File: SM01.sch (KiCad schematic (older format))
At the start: 37 parts

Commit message: basic layout complete
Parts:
- removed J?: SynthOut, symbol JACK-MONO
- removed J?: DC JACK, symbol JACK-MONO
- removed R?: R, symbol R
- removed U? (x5): 74AHC1G14, symbol 74AHC1G14
- added ATTACK, ATTACK? (x2), DECAY, DECAY? (x2): A500k, symbol POT
- added C3, C?: 100uF, C-POL-5, symbol CAP-ELEC-TH
- added C? (x2): C, symbol C
- added C? (x3): 10uF, symbol C
- added C? (x10): 1uF, symbol C
- added C? (x5): .1uF, symbol C
- added C? (x2): .22uF, symbol C
- added C? (x4): 47pF, symbol C
- added D2, D? (x2): 4148, symbol D
- added D?: D, symbol D
- added J2, J? (x2): TRIG IN, symbol JACK-MONO
- added J?: VCA IN, symbol JACK-MONO
- added J?: EXP1, symbol JACK-MONO
- added J?: EXP2, symbol JACK-MONO
- added J?: EXP3, symbol JACK-MONO
- added LED? (x2): LED-C1-A2, LED-C1-A2-3MM-VERT, symbol LED-C1-A2
- added MOM1, SW4, SW? (x2): SPDT_small, symbol SPDT_small
- added OSC? (x2): 10k, symbol POT
- added Q?: 2N3904, TO_SOT_Packages_THT:TO-92_Molded_Narrow, symbol 2N3904
- added R1, R2, R? (x15): 100k, symbol R
- added R3, R? (x2): 1k, symbol R
- added R4, R? (x7): 10k, symbol R
- added R5, R? (x2): 200k, symbol R
- added R? (x8): R, symbol R
- added R? (x2): 470, symbol R
- added R? (x4): 100k, 100k, symbol R
- added R?: R, 100k, symbol R
- added SW2, SW? (x9): MOM, symbol SPDT_small
- added SW3, SW? (x2): HOLD, symbol SPDT_small
- added U, U1, U? (x10): LM324, symbol LM324
- added U1, U? (x16): HEX_INV_TRI, symbol HEX_INV_TRI
- added VOL1, VOL? (x3): 10k, 10k, symbol POT
- C1: renamed from C?; value CAP-ELEC-TH -> 100uF
- C2: renamed from C?; value CAP-ELEC-TH -> 10uF
- C? (x2): value C -> 1uF
- C?: value C -> .1uF
- C?: value C -> .22uF
- OSC1: renamed from RV?; value POT -> 10k
- R? (x2): value R -> 100k
- R?: value R -> 10k
- R?: value R -> 470
- SW1: renamed from SW?; value SWITCH_INV -> ON
- gave numbers to parts that had none: 4
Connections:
- net labels added: 2.5V, 2.5v, DONTFORGETTOASSIGNMIXEROPAMPS, OSC1
- wire segments 57 -> 286
- no-connect marks 15 -> 28
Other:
- moved on the sheet: C1, C2, C?, D1, D?, HOLD, J1, J?, LED?, OSC1, R?, RV?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

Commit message: finished one full channel and vca channel
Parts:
- removed ATTACK? (x2), DECAY? (x2): A500k, symbol POT
- removed C? (x3): C, symbol C
- removed C? (x8): 1uF, symbol C
- removed C? (x4): .1uF, symbol C
- removed C? (x2): .22uF, symbol C
- removed C? (x2): 10uF, symbol C
- removed C? (x4): 47pF, symbol C
- removed D?: D, symbol D
- removed D? (x2): 4148, symbol D
- removed HOLD, MOM1, SW? (x3): SPDT_small, symbol SPDT_small
- removed J? (x3): TRIG IN, symbol JACK-MONO
- removed J?: EXP1, symbol JACK-MONO
- removed J?: EXP2, symbol JACK-MONO
- removed J?: EXP3, symbol JACK-MONO
- removed LED? (x2): LED-C1-A2, LED-C1-A2-3MM-VERT, symbol LED-C1-A2
- removed OSC? (x2): 10k, symbol POT
- removed R? (x9): R, symbol R
- removed R? (x12): 100k, symbol R
- removed R? (x6): 10k, symbol R
- removed R? (x2): 470, symbol R
- removed R? (x2): 1k, symbol R
- removed R? (x2): 200k, symbol R
- removed R? (x3): 100k, 100k, symbol R
- removed RV?: POT, symbol POT
- removed SW? (x2): HOLD, symbol SPDT_small
- removed SW? (x7): MOM, symbol SPDT_small
- removed U, U? (x12): LM324, symbol LM324
- removed U? (x14): HEX_INV_TRI, symbol HEX_INV_TRI
- removed VOL? (x3): 10k, 10k, symbol POT
- added ATTACK?, DECAY?: A500k, 4ms-footprints:POT-9MM-ALPHA, symbol POT
- added C16: 10uF, 4ms-footprints:Cap_Electrolytic_TH, symbol CAP-ELEC-TH
- added C?: 10uF, 4ms-footprints:Cap_Ceramic_TH, symbol C
- added C?: 1uF, 4ms-footprints:Cap_Ceramic_TH, symbol C
- added D?: 4148, 4ms-footprints:Diode_BAT-85S_TH, symbol D
- added J5: MIXOUT, zfoot:Jack_Instrument, symbol JACK-TIP_GND
- added J?: TRIG IN, zfoot:Jack_Instrument, symbol JACK-TIP_GND
- added MASTERV1: A100k, 4ms-footprints:POT-9MM-ALPHA, symbol POT
- added R? (x2): 1k, 4ms-footprints:Resistor_TH_300, symbol R
- added R?: 200k, 4ms-footprints:Resistor_TH_300, symbol R
- added R? (x3): 10k, 4ms-footprints:Resistor_TH_300, symbol R
- added R? (x7): 100k, 4ms-footprints:Resistor_TH_300, symbol R
- added SENSE1, SENSE?: A50k, 4ms-footprints:POT-9MM-ALPHA, symbol POT
- added SW7: MASTERSW, 4ms-footprints:SPDT-SUB, symbol SPDT_small
- added SW?: SPDT_small, 4ms-footprints:SPDT-SUB, symbol SPDT_small
- added SW?: HOLD, 4ms-footprints:SPDT-SUB, symbol SPDT_small
- added SW? (x4): MOM, 4ms-footprints:SPDT-SUB, symbol SPDT_small
- added U3, U4, U5, U7: 072, 4ms-footprints:DIP_8pin_TL072_TH, symbol TL072
- added VOL? (x3): 10k, 4ms-footprints:POT-9MM-ALPHA, symbol POT
- ATTACK1: renamed from ATTACK; footprint (none) -> 4ms-footprints:POT-9MM-ALPHA
- C1, C2, C3: footprint C-POL-5 -> 4ms-footprints:Cap_Electrolytic_TH
- C10, C12, C4, C5, C9: renamed from C?; footprint (none) -> 4ms-footprints:Cap_Ceramic_TH
- C13, C6, C7: renamed from C?; footprint (none) -> 4ms-footprints:Cap_Electrolytic_TH; symbol C -> CAP-ELEC-TH
- C15: renamed from C?; value 100uF -> 10uF; footprint C-POL-5 -> 4ms-footprints:Cap_Electrolytic_TH
- C8: renamed from C?; value C -> 100nF; footprint (none) -> 4ms-footprints:Cap_Ceramic_TH
- D1: footprint SMA -> 4ms-footprints:Diode_BAT-85S_TH
- D2: footprint (none) -> 4ms-footprints:Diode_BAT-85S_TH
- D3: renamed from D?; value D -> 4148; footprint (none) -> 4ms-footprints:Diode_BAT-85S_TH
- DECAY1: renamed from DECAY; footprint (none) -> 4ms-footprints:POT-9MM-ALPHA
- J1: footprint (none) -> zfoot:Jack_DC; symbol JACK-MONO -> JACK-DC
- J2: footprint (none) -> zfoot:Jack_Instrument; symbol JACK-MONO -> JACK-TIP_GND
- J3: renamed from J?; footprint (none) -> zfoot:Jack_Instrument; symbol JACK-MONO -> JACK-TIP_GND
- LED1: renamed from LED?; footprint LED-C1-A2-3MM-VERT -> 4ms-footprints:LED-C1-A2-3MM-VERT; symbol LED-C1-A2 -> LED
- OSC1: footprint (none) -> 4ms-footprints:POT-9MM-ALPHA
- Q1: renamed from Q?; footprint TO_SOT_Packages_THT:TO-92_Molded_Narrow -> 4ms-footprints:TO-92_Molded_Narrow
- R1, R2, R3, R4, R5: footprint (none) -> 4ms-footprints:Resistor_TH_300
- R10: renamed from R?; value R -> 1k; footprint (none) -> 4ms-footprints:Resistor_TH_300
- R11: renamed from R?; value R -> 10k; footprint (none) -> 4ms-footprints:Resistor_TH_300
- R12, R13, R14, R16, R6, R7, R8: renamed from R?; footprint (none) -> 4ms-footprints:Resistor_TH_300
- R15: renamed from R?; value 100k -> 10k; footprint (none) -> 4ms-footprints:Resistor_TH_300
- R17: renamed from R?; footprint 100k -> 4ms-footprints:Resistor_TH_300
- R18: renamed from R?; value R -> 100k; footprint 100k -> 4ms-footprints:Resistor_TH_300
- R9: renamed from R?; value R -> 100k; footprint (none) -> 4ms-footprints:Resistor_TH_300
- SW1: footprint (none) -> 4ms-footprints:SPDT-SUB; symbol SWITCH_INV -> SPDT_small
- SW2, SW3, SW4: footprint (none) -> 4ms-footprints:SPDT-SUB
- SW5, SW6: renamed from SW?; footprint (none) -> 4ms-footprints:SPDT-SUB
- U1: value LM324 -> 072; footprint (none) -> 4ms-footprints:DIP_8pin_TL072_TH; symbol LM324 -> TL072
- U2: renamed from U1; value HEX_INV_TRI -> 7414; footprint (none) -> 4ms-footprints:DIP-14_W7.62mm
- U2: renamed from U?; value HEX_INV_TRI -> 7414; footprint (none) -> 4ms-footprints:DIP-14_W7.62mm
- VOL1: footprint 10k -> 4ms-footprints:POT-9MM-ALPHA
- VREG1: renamed from VREG; footprint (none) -> 4ms-footprints:Regulator_5V_7805_LARGE_TH
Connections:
- net labels removed: DONTFORGETTOASSIGNMIXEROPAMPS, OSC1
- wire segments 286 -> 156
- no-connect marks 28 -> 13
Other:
- note added: "OPTIONAL!"
- note added: "optional"
- moved on the sheet: C15, C8, D3, Q1, R10, R11, R18, R9

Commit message: sorting PCB page
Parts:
- added ATTACK2, ATTACK3, DECAY2, DECAY3: A500k, 4ms-footprints:POT-9MM-ALPHA, symbol POT
- added C11, C12, C14, C15, C29, C30: 1uF, 4ms-footprints:Cap_Electrolytic_TH, symbol CAP-ELEC-TH
- added C19, C20, C22, C23: .1uF, 4ms-footprints:Cap_Ceramic_TH, symbol C
- added C26, C27: .22uF, 4ms-footprints:Cap_Ceramic_TH, symbol C
- added C5, C6: 1uF, 4ms-footprints:Cap_Ceramic_TH, symbol C
- added C8, C9: 10uF, 4ms-footprints:Cap_Ceramic_TH, symbol C
- added D3, D4: 4148, 4ms-footprints:Diode_BAT-85S_TH, symbol D
- added J2, J3: TRIG IN, zfoot:Jack_Instrument, symbol JACK-TIP_GND
- added LED2, LED3: LED-C1-A2, 4ms-footprints:LED-C1-A2-3MM-VERT, symbol LED
- added OSC2, OSC3: 10k, 4ms-footprints:POT-9MM-ALPHA, symbol POT
- added R10, R11: 200k, 4ms-footprints:Resistor_TH_300, symbol R
- added R13, R14: 470, 4ms-footprints:Resistor_TH_300, symbol R
- added R16, R17, R22, R23, R25, R26: 100k, 4ms-footprints:Resistor_TH_300, symbol R
- added R2, R3: 1k, 4ms-footprints:Resistor_TH_300, symbol R
- added R29, R30, R32, R33, R5, R6: 10k, 4ms-footprints:Resistor_TH_300, symbol R
- added SENSE2, SENSE3: A50k, 4ms-footprints:POT-9MM-ALPHA, symbol POT
- added SW10, SW11: SPDT_small, 4ms-footprints:SPDT-SUB, symbol SPDT_small
- added SW15, SW16, SW6, SW7: MOM, 4ms-footprints:SPDT-SUB, symbol SPDT_small
- added SW2, SW3: HOLD, 4ms-footprints:SPDT-SUB, symbol SPDT_small
- added U2, U3: 072, 4ms-footprints:DIP_8pin_TL072_TH, symbol TL072
- added U5, U6: 7414, 4ms-footprints:DIP-14_W7.62mm, symbol HEX_INV_TRI
- gave numbers to parts that had none: 29
- renumbered C6 to C10, C7 to C13, C9 to C18, C10 to C21, C8 to C24, C12 to C25, C13 to C28, C16 to C31, C15 to C32, C5 to C7, D3 to D6, J2 to J1, J1 to J4, J3 to J6, J5 to J7, R3 to R1, R14 to R12, R6 to R15, R7 to R21, R8 to R24, R12 to R28, R13 to R31, R9 to R34, R10 to R35, R11 to R36, R15 to R37, R16 to R41, R17 to R45, R18 to R48, R1 to R7, R2 to R8, R5 to R9, SW3 to SW1, SW5 to SW14, SW6 to SW18, SW7 to SW21, SW1 to SW4, SW2 to SW5, SW4 to SW9, U3 to U10, U4 to U11, U2 to U4, U7 to U8, U5 to U9, VOL1 to VOL2
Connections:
- net +5V: now also SW2.2, SW3.2, SW6.2, SW7.2, U2.8 (V+), U3.8 (V+)
- net GND: now also C11.2 (-), C12.2 (-), C14.2 (-), C15.2 (-), C29.2 (-), C30.2 (-), C5.1, C6.1, C8.2, C9.2, DECAY2.2 (Center), DECAY2.3 (Right), DECAY3.2 (Center), DECAY3.3 (Right), J2.2 (GND), J3.2 (GND), LED2.2 (C), LED3.2 (C), R5.2, R6.2, SENSE2.3 (Right), SENSE3.3 (Right), U2.4 (V-), U3.4 (V-), U5.7, U5.9, U6.7, U6.9
- net at R38.1: now also OSC2.3 (Right), U5.6
- net at R39.1: now also OSC3.3 (Right), U6.6
- new net: C14.1 (+), R25.1, U5.1
- new net: C22.2, R25.2, U5.2
- new net: C22.1, R32.1, U5.3
- new net: R32.2, SW15.3, U5.4
- new net: C26.1, C29.1 (+), OSC2.1 (Left), OSC2.2 (Center), U5.5
- new net: C26.2, SW15.2
- new net: R13.1, U5.8
- new net: LED2.1 (A), R13.2
- new net: J2.1 (V), SENSE2.1 (Left)
- new net: R2.1, SW2.3, SW6.1
- new net: R2.2, SENSE2.2 (Center), U2.3 (+)
- new net: D3.2 (A), R10.1, U2.1
- new net: R10.2, R5.1, U2.2 (-)
- new net: ATTACK2.2 (Center), ATTACK2.3 (Right), R16.1, SW10.2, U2.5 (+)
- new net: U2.6 (-), U2.7, U5.14
- new net: ATTACK2.1 (Left), D3.1 (K)
- new net: C8.1, SW10.1
- new net: C5.2, SW10.3
- new net: DECAY2.1 (Left), R16.2
- new net: C11.1 (+), R22.1, U5.14
- new net: C19.2, R22.2, U5.13
- new net: C19.1, R29.1, U5.11
- new net: R29.2, SW15.1, U5.10
- new net: C15.1 (+), R26.1, U6.1
- new net: C23.2, R26.2, U6.2
- new net: C23.1, R33.1, U6.3
- new net: R33.2, SW16.3, U6.4
- new net: C27.1, C30.1 (+), OSC3.1 (Left), OSC3.2 (Center), U6.5
- new net: C27.2, SW16.2
- new net: R14.1, U6.8
- new net: LED3.1 (A), R14.2
- new net: J3.1 (V), SENSE3.1 (Left)
- new net: R3.1, SW3.3, SW7.1
- new net: R3.2, SENSE3.2 (Center), U3.3 (+)
- new net: D4.2 (A), R11.1, U3.1
- new net: R11.2, R6.1, U3.2 (-)
- new net: ATTACK3.2 (Center), ATTACK3.3 (Right), R17.1, SW11.2, U3.5 (+)
- new net: U3.6 (-), U3.7, U6.14
- new net: ATTACK3.1 (Left), D4.1 (K)
- new net: C9.1, SW11.1
- new net: C6.2, SW11.3
- new net: DECAY3.1 (Left), R17.2
- new net: C12.1 (+), R23.1, U6.14
- new net: C20.2, R23.2, U6.13
- new net: C20.1, R30.1, U6.11
- new net: R30.2, SW16.1, U6.10
- no-connect marks 13 -> 17
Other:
- moved on the sheet: LED1, R12, U4D

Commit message: continued laying out pcb - having issue with zfoot.pretty
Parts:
- removed LED1, LED2, LED3: LED-C1-A2, 4ms-footprints:LED-C1-A2-3MM-VERT, symbol LED
- removed SW12, SW5, SW6, SW7: MOM, 4ms-footprints:SPDT-SUB, symbol SPDT_small
- added LEDSW1, LEDSW2, LEDSW3, LEDSW4: DPDT-ILLUM, 4ms-footprints:BUTTON-LED-PB61303, symbol DPDT-ILLUM
- added R50: 470, 4ms-footprints:Resistor_TH_300, symbol R
- SW10: value SPDT_small -> DECAYSW2
- SW11: value SPDT_small -> DECAYSW3
- SW13: value SPDT_small -> DECAYSW4
- SW14: value MOM -> OSCSW1
- SW15: value MOM -> OSCSW2
- SW16: value MOM -> OSCSW3
- SW17: value MOM -> MUTE4
- SW18: value MOM -> MUTE1
- SW19: value MOM -> MUTE2
- SW20: value MOM -> MUTE3
- SW9: value SPDT_small -> DECAYSW1
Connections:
- net +5V: now also LEDSW1.3 (DOWN-A), LEDSW2.3 (DOWN-A), LEDSW3.3 (DOWN-A), LEDSW4.3 (DOWN-A)
- net GND: now also LEDSW1.8 (C), LEDSW2.8 (C), LEDSW3.8 (C), LEDSW4.8 (C)
- net at R12.2: now also LEDSW1.7 (A)
- net at J1.1 (V), SENSE1.1 (Left): now also R1.1, SW1.3, LEDSW1.2 (POLE-A)
- net at R13.2: now also LEDSW2.7 (A)
- net at J2.1 (V), SENSE2.1 (Left): now also R2.1, SW2.3, LEDSW2.2 (POLE-A)
- net at R14.2: now also LEDSW3.7 (A)
- net at J3.1 (V), SENSE3.1 (Left): now also R3.1, SW3.3, LEDSW3.2 (POLE-A)
- net at J5.1 (V), SENSE4.1 (Left): now also R18.1, SW8.3, LEDSW4.2 (POLE-A)
- net at ATTACK4.2 (Center), ATTACK4.3 (Right), R27.1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: now also U11.5 (+)
- net LED_AR: now reaches U11.6 (-)
- net LED_AR: now also U11.7, R50.1
- new net: LEDSW4.7 (A), R50.2
- no-connect marks 17 -> 27
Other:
- moved on the sheet: ATTACK1, ATTACK2, ATTACK3, ATTACK4, C1, C10, C11, C12, C13, C14, C15, C16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

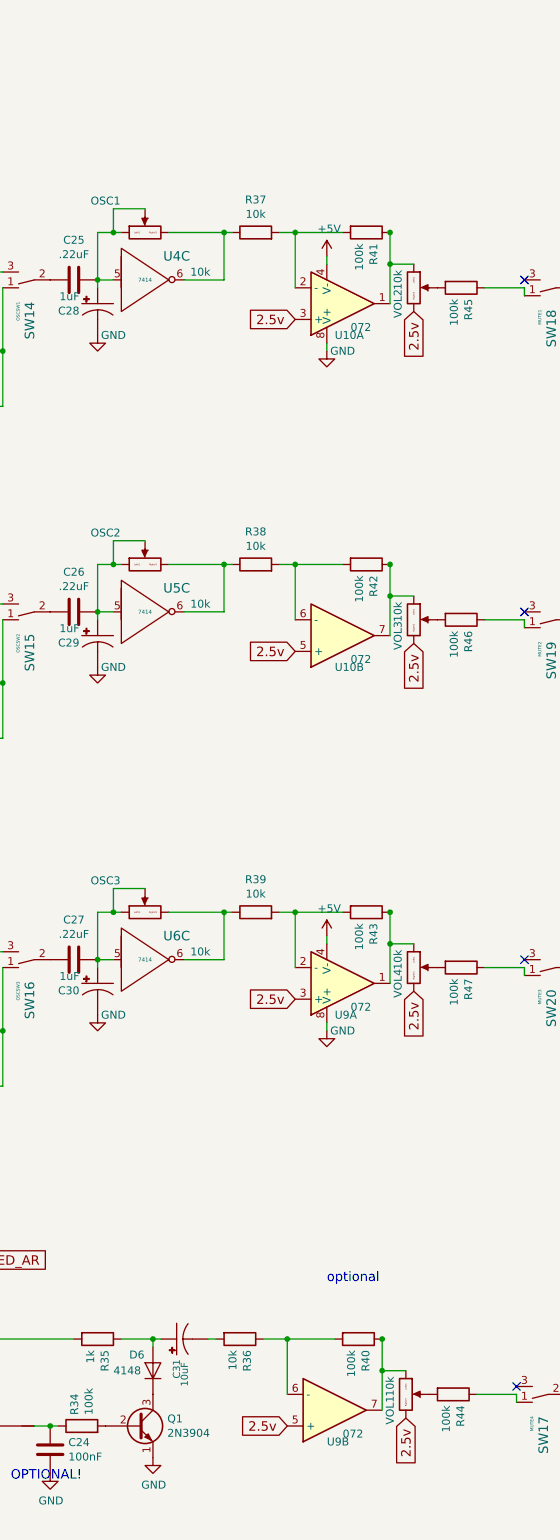
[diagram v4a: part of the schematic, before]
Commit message: finished placing components - starting to connect traces
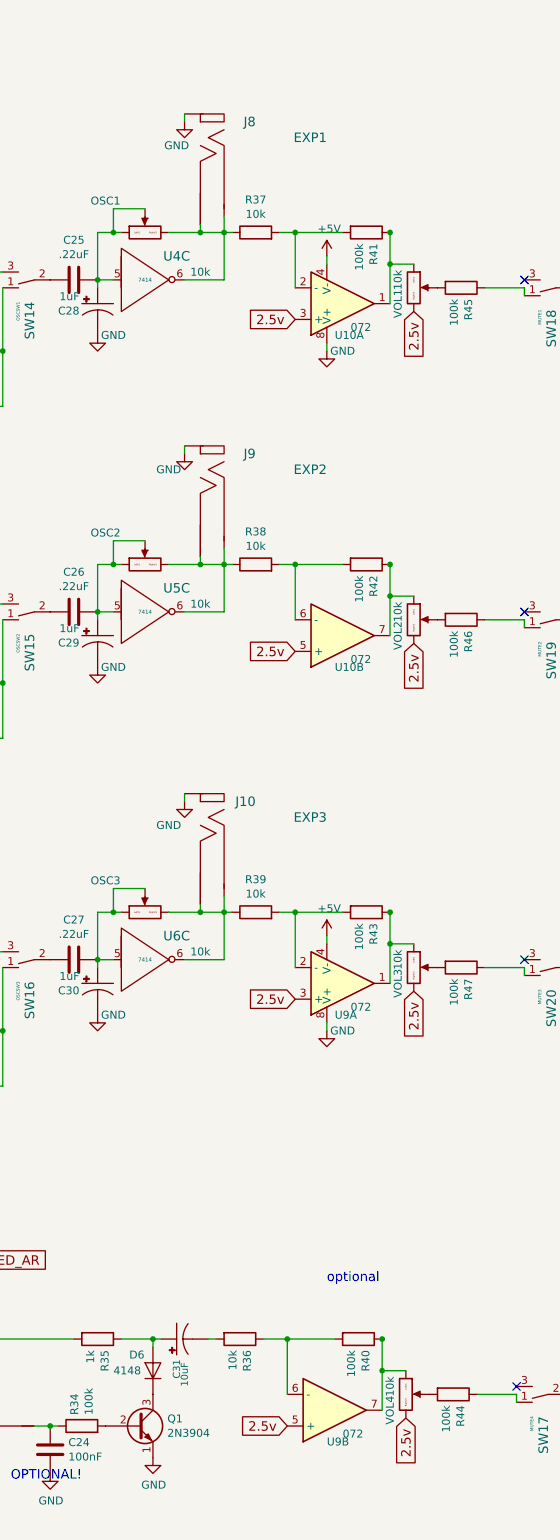
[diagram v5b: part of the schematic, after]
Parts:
- added J10: EXP3, zfoot:Jack_Instrument_exp, symbol JACK-STEREO
- added J8: EXP1, zfoot:Jack_Instrument_exp, symbol JACK-STEREO
- added J9: EXP2, zfoot:Jack_Instrument_exp, symbol JACK-STEREO
- renumbered VOL2 to VOL1, VOL3 to VOL2, VOL4 to VOL3, VOL1 to VOL4
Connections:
- net GND: now also J10.3 (SHEILD), J8.3 (SHEILD), J9.3 (SHEILD)
- net at OSC1.3 (Right), R37.1, U4.6: now also J8.1 (SW), J8.2 (SIG)
- net at OSC2.3 (Right), R38.1, U5.6: now also J9.1 (SW), J9.2 (SIG)
- net at OSC3.3 (Right), R39.1, U6.6: now also J10.1 (SW), J10.2 (SIG)
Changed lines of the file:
@@
 $EndComp
 $Comp
-L POT VOL2
+L POT VOL1
 U 1 1 59A4A330
 P 11400 1900
-F 0 "VOL2" V 11300 1800 50  0000 C CNN
+F 0 "VOL1" V 11300 1800 50  0000 C CNN
 F 1 "10k" V 11300 1950 50  0000 C CNN
 F 2 "4ms-footprints:POT-9MM-ALPHA" H 11600 1650 50  0001 C CNN
@@
 $EndComp
 $Comp
-L POT VOL3
+L POT VOL2
 U 1 1 59AD57AE
 P 11400 4000
-F 0 "VOL3" V 11300 3900 50  0000 C CNN
+F 0 "VOL2" V 11300 3900 50  0000 C CNN
 F 1 "10k" V 11300 4050 50  0000 C CNN
 F 2 "4ms-footprints:POT-9MM-ALPHA" H 11600 3750 50  0001 C CNN
@@
 $EndComp
 $Comp
-L POT VOL4
+L POT VOL3
 U 1 1 59AD6F8E
 P 11400 6200
-F 0 "VOL4" V 11300 6100 50  0000 C CNN
+F 0 "VOL3" V 11300 6100 50  0000 C CNN
 F 1 "10k" V 11300 6250 50  0000 C CNN
 F 2 "4ms-footprints:POT-9MM-ALPHA" H 11600 5950 50  0001 C CNN
@@
 $EndComp
 $Comp
-L POT VOL1
+L POT VOL4
 U 1 1 59AD8492
 P 11350 8900
-F 0 "VOL1" V 11250 8800 50  0000 C CNN
+F 0 "VOL4" V 11250 8800 50  0000 C CNN
 F 1 "10k" V 11250 8950 50  0000 C CNN
 F 2 "4ms-footprints:POT-9MM-ALPHA" H 11550 8650 50  0001 C CNN
@@
 Text GLabel 4100 7700 0    60   Input ~ 0
 LED_AR
+$Comp
+L JACK-STEREO J8
+U 1 1 59AB9E9D
+P 10050 950
+F 0 "J8" V 9950 1300 60  0000 R CNN
+F 1 "EXP1" V 10050 1750 60  0000 R CNN
+F 2 "zfoot:Jack_Instrument_exp" H 10250 1194 60  0001 C CNN
+F 3 "" H 10050 950 60  0000 C CNN
+	1    10050 950
+	0    1    1    0
+$EndComp
+$Comp
+L GND #PWR072
+U 1 1 59ACB737
+P 9950 850
+F 0 "#PWR072" H 9950 600 50  0001 C CNN
+F 1 "GND" H 9900 700 50  0000 C CNN
+F 2 "" H 9950 850 50  0001 C CNN
+F 3 "" H 9950 850 50  0001 C CNN
+	1    9950 850
+	1    0    0    -1
+$EndComp
 Wire Wire Line
 	1500 10100 1600 10100
@@
 	9850 1550 10250 1550
 Wire Wire Line
-	10200 1550 10200 1850
+	10200 1450 10200 1850
 Wire Wire Line
 	9700 1400 9500 1400
@@
 	3400 4100 3400 4150
 Wire Wire Line
-	10200 3950 10200 3650
+	10200 3550 10200 3950
 Connection ~ 10200 3650
 Wire Wire Line
@@
 	3400 6300 3400 6350
 Wire Wire Line
-	10200 6150 10200 5850
+	10200 5750 10200 6150
 Connection ~ 10200 5850
 Wire Wire Line
@@
 	5200 8450 5200 8350
 Connection ~ 5200 8350
+Wire Wire Line
+	10050 1500 10050 1550
+Connection ~ 10050 1550
+Wire Wire Line
+	9950 800  9950 850
+$Comp
+L JACK-STEREO J9
+U 1 1 59AD4C65
+P 10050 3050
+F 0 "J9" V 9950 3400 60  0000 R CNN
+F 1 "EXP2" V 10050 3850 60  0000 R CNN
+F 2 "zfoot:Jack_Instrument_exp" H 10250 3294 60  0001 C CNN
+F 3 "" H 10050 3050 60  0000 C CNN
+	1    10050 3050
+	0    1    1    0
+$EndComp
+$Comp
+L GND #PWR073
+U 1 1 59AD4C6B
+P 9950 2950
+F 0 "#PWR073" H 9950 2700 50  0001 C CNN
+F 1 "GND" H 9850 2850 50  0000 C CNN
+F 2 "" H 9950 2950 50  0001 C CNN
+F 3 "" H 9950 2950 50  0001 C CNN
+	1    9950 2950
+	1    0    0    -1
+$EndComp
+Wire Wire Line
+	9950 2900 9950 2950
+$Comp
+L JACK-STEREO J10
+U 1 1 59AD679A
+P 10050 5250
+F 0 "J10" V 9950 5600 60  0000 R CNN
+F 1 "EXP3" V 10050 6050 60  0000 R CNN
+F 2 "zfoot:Jack_Instrument_exp" H 10250 5494 60  0001 C CNN
+F 3 "" H 10050 5250 60  0000 C CNN
+	1    10050 5250
+	0    1    1    0
+$EndComp
+$Comp
+L GND #PWR074
+U 1 1 59AD67A0
+P 9950 5150
+F 0 "#PWR074" H 9950 4900 50  0001 C CNN
+F 1 "GND" H 9850 5000 50  0000 C CNN
+F 2 "" H 9950 5150 50  0001 C CNN
+F 3 "" H 9950 5150 50  0001 C CNN
+	1    9950 5150
+	1    0    0    -1
+$EndComp
+Wire Wire Line
+	9950 5100 9950 5150
+Wire Wire Line
+	10050 5800 10050 5850
+Connection ~ 10050 5850
+Wire Wire Line
+	10050 3600 10050 3650
+Connection ~ 10050 3650
 $EndSCHEMATC

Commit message: finished channel 1 but theres so much more bullshit left
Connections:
- net at J8.2 (SIG), R37.1, U4.6: no longer J8.1 (SW), OSC1.3 (Right)
- net at J9.2 (SIG), R38.1, U5.6: no longer J9.1 (SW), OSC2.3 (Right)
- net at J10.2 (SIG), R39.1, U6.6: no longer J10.1 (SW), OSC3.3 (Right)
- new net: J8.1 (SW), OSC1.3 (Right)
- new net: J9.1 (SW), OSC2.3 (Right)
- new net: J10.1 (SW), OSC3.3 (Right)

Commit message: fixed 2.5v tag issue
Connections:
- net 2.5V is gone; now on net 2.5v: C3.1 (+), R7.2, R8.1
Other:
- moved on the sheet: ATTACK1, ATTACK2, ATTACK3, ATTACK4, C1, C10, C11, C12, C13, C14, C15, C16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
